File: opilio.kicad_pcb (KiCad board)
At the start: 4 copper layers, 75 x 46 mm, 113 parts, among them J1 Conn_01x04_Male, J2 SATA_Power_Connector, J3 USB_C_Receptacle_USB2.0, J4 Conn_01x06_Male, Q1 CJ3134KW, Q2 AO3401A, Q3 CJ3134KW, Q4 AO3401A, SW1 TS-1077S-01726, SW2 TS-1077S-01726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

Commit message: cleanup
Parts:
- added kibuzzard-638B7105: G***, kibuzzard-638B7105, F.Cu at (109.0, 126.7)
- added kibuzzard-638B7145: G***, kibuzzard-638B7145, F.Cu at (109.6, 130.1)
- added kibuzzard-638BCC66: G***, kibuzzard-638BCC66, F.Cu at (118.7, 99.1)
- moved kibuzzard-63853CA9 1.31 mm to (143.7, 127.1)
- moved kibuzzard-63853BC6 0.16 mm to (117.4, 102.2)
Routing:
- net GND: track 98.2 -> 96.7 mm, vias 82 -> 87
- net WATER_OUT_T: track 17.0 -> 16.3 mm
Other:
- board text added: "3v3"
- board text removed: "VID 0x1209 PID 0x2442"

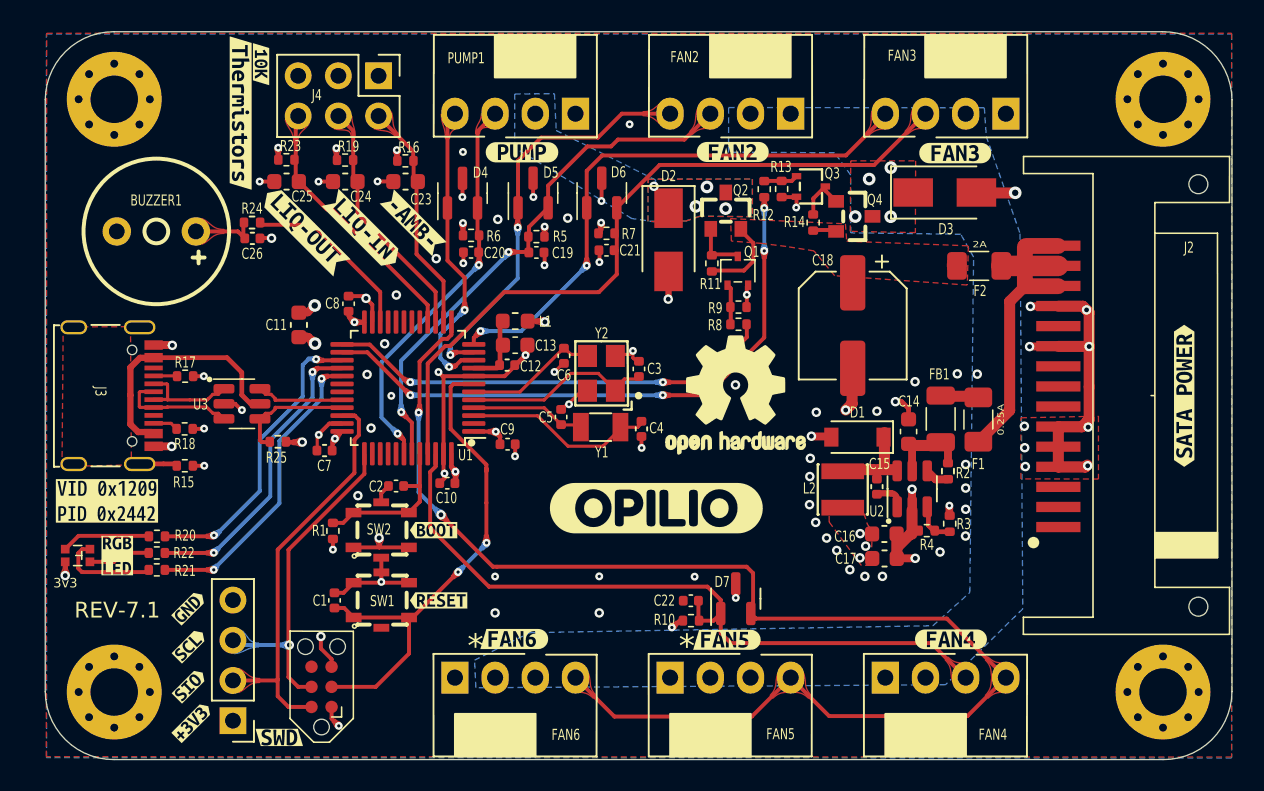
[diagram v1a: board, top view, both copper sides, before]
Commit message: move buzzer and teardrop
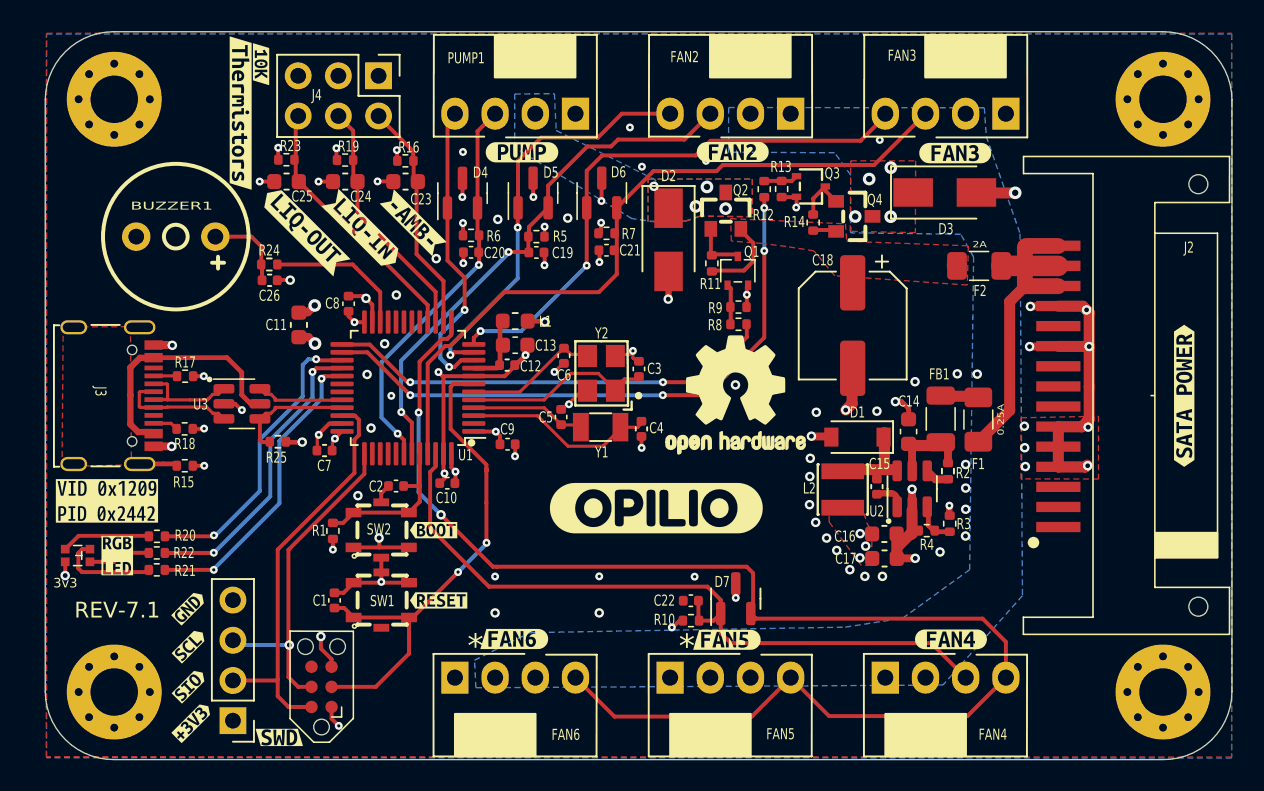
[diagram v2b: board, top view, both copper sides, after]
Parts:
- moved C26 2.87 mm to (119.3, 112.7)
- moved R24 2.87 mm to (119.2, 111.7)
- moved BUZZER1 1.27 mm to (113.3, 110.0)
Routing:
- net BUZZER: track 11.3 -> 9.13 mm
- net PWM_OUT4: track 86.5 -> 87.8 mm
- net Net-(BUZZER1-Pad1): track 4.24 -> 5.32 mm
- net GND: vias 87 -> 91

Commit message: Initial stl files working
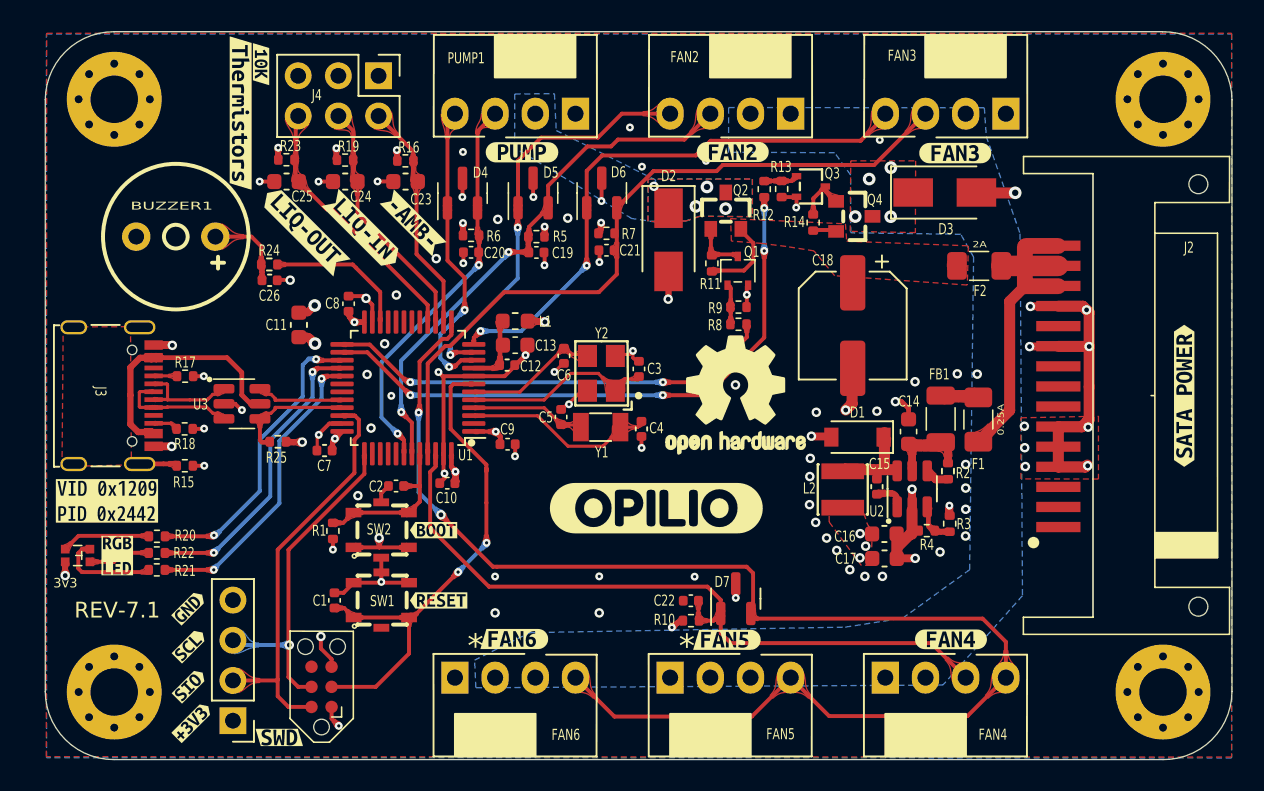
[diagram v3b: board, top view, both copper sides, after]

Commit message: kicad - 7
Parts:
- removed kibuzzard-63853BFA: G***, kibuzzard-63853BFA
- removed kibuzzard-63853C04: G***, kibuzzard-63853C04
- removed kibuzzard-638555C7: G***, kibuzzard-638555C7
- removed kibuzzard-638555D0: G***, kibuzzard-638555D0
- removed kibuzzard-638555D8: G***, kibuzzard-638555D8
- added kibuzzard-63BAEB9A: G***, kibuzzard-63BAEB9A, F.Cu at (123.4, 99.1)
- added kibuzzard-63BAEBBB: G***, kibuzzard-63BAEBBB, F.Cu at (128.5, 99.1)
- added kibuzzard-63BAEC58: G***, kibuzzard-63BAEC58, F.Cu at (126.0, 99.1)
- added kibuzzard-63BAF879: G***, kibuzzard-63BAF879, F.Cu at (126.1, 131.3)
- added kibuzzard-63BAF885: G***, kibuzzard-63BAF885, F.Cu at (133.8, 131.3)
- J4: footprint Connector_PinHeader_2.54mm:PinHeader_2x03_P2.54mm_Vertical -> easyeda2kicad:HDR-TH_6P-P2.54-H-M-R2-C3-S2.54
- moved SW1 8.83 mm to (133.9, 128.4), turned to 180 degrees
- moved C1 7.30 mm to (126.2, 139.7), turned to -90 degrees
- moved J4 7.03 mm to (124.7, 106.7), turned to 180 degrees
- moved R23 6.31 mm to (121.5, 111.3)
- moved R19 6.22 mm to (124.8, 111.3)
- moved R16 6.12 mm to (127.9, 111.3)
- moved C25 3.48 mm to (121.0, 109.9)
- moved C23 3.45 mm to (127.5, 109.9)
- moved C24 3.44 mm to (124.3, 109.9)
- moved kibuzzard-638BCC66 1.43 mm to (120.2, 99.2)
- moved kibuzzard-63853BC6 1.42 mm to (118.8, 102.2)
- moved R24 1.37 mm to (119.2, 113.1)
- moved C26 0.91 mm to (119.2, 111.8)
- moved R13 0.18 mm to (151.4, 107.0)
- moved C8 0.15 mm to (124.2, 114.4)
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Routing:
- net AMBIENT_T: track 14.4 -> 8.96 mm
- net NRST: track 34.6 -> 30.1 mm
- net WATER_IN_T: track 15.3 -> 11.0 mm
- net GND: track 96.7 -> 93.3 mm, vias 91 -> 89
- net PWM_OUT4: track 87.8 -> 90.9 mm
- net WATER_OUT_T: track 16.3 -> 13.4 mm
- net PWM_READ4: track 46.6 -> 47.8 mm
- net BUZZER: track 9.13 -> 8.57 mm
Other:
- board text added: "REV-7.2"
- board text removed: "REV-7.1"

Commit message: enclosure update
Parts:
- moved LOGO1 25.2 mm to (131.6, 138.5)
- moved kibuzzard-63853C0D 8.94 mm to (143.7, 135.4)
- moved FAN6 7.40 mm to (142.2, 137.8)
- moved PUMP1 7.40 mm to (142.2, 102.2)
- moved kibuzzard-63853C81 7.18 mm to (142.4, 104.5)
- moved kibuzzard-638559F0 6.74 mm to (154.9, 135.4)
- moved kibuzzard-63853C76 5.62 mm to (154.2, 104.7)
- moved FAN2 5.00 mm to (153.4, 102.2)
- moved FAN5 5.00 mm to (153.4, 137.8)
- moved FAN3 2.60 mm to (164.6, 102.2)
- moved FAN4 2.60 mm to (164.6, 137.8)
- moved kibuzzard-638559F7 2.43 mm to (164.8, 135.4)
- moved kibuzzard-63853C6A 1.96 mm to (164.6, 104.7)
- moved kibuzzard-63853CA9 0.80 mm to (144.3, 126.7)
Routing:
- net PWM_OUT2: track 26.4 -> 38.5 mm, vias 2 -> 3
- net PWM_OUT1: track 18.6 -> 30.0 mm, vias 2 -> 3
- net PWM_READ1: track 25.0 -> 33.4 mm
- net PWM_READ2: track 33.9 -> 39.8 mm
- net PWM_OUT4: track 90.9 -> 85.6 mm
- net PWM_READ4: track 47.8 -> 50.4 mm
- net PWM_OUT3: track 35.7 -> 38.3 mm
- net PWM_READ3: track 46.2 -> 48.6 mm
- net GND: track 93.3 -> 92.9 mm, vias 89 -> 85
- net 12vP: vias 4 -> 3

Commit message: wip migrate to kicad 7
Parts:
- moved kibuzzard-638559F7 0.12 mm to (164.6, 135.4)
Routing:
- net NRST: track 30.1 -> 31.1 mm

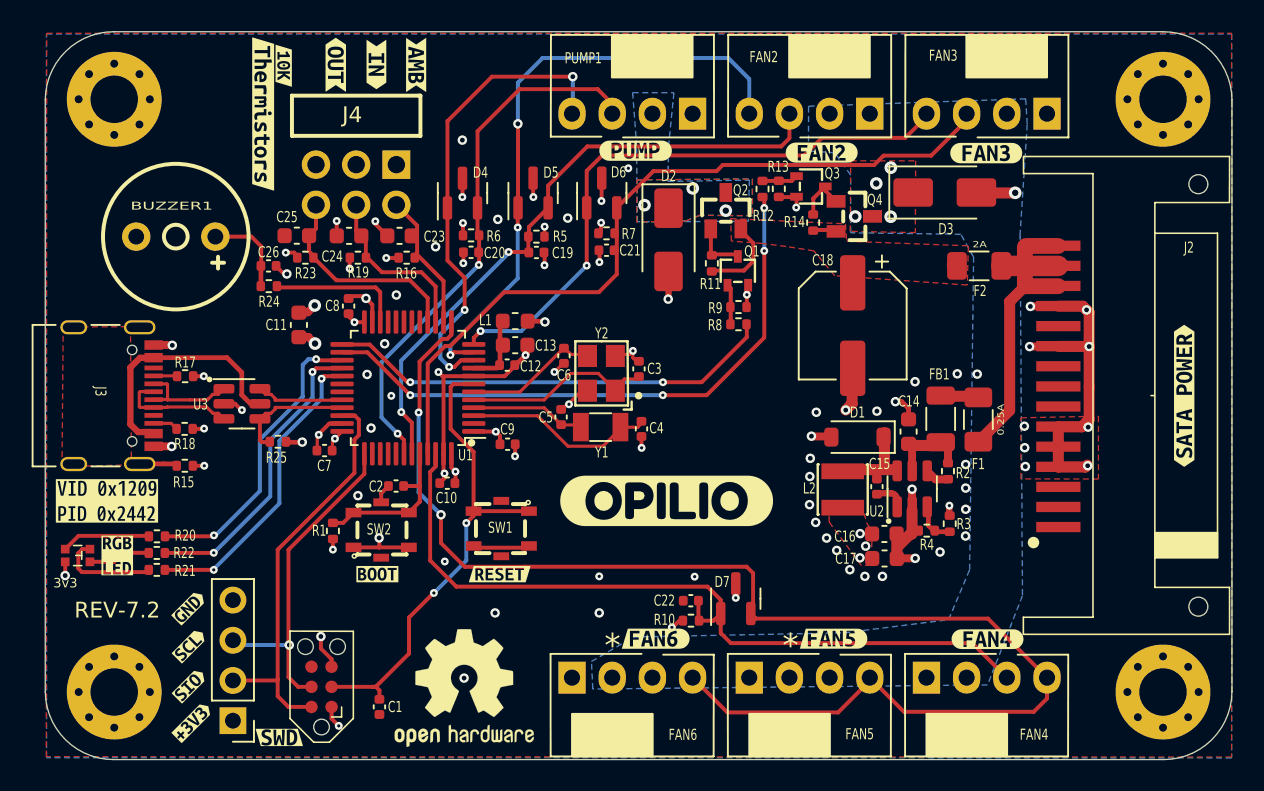
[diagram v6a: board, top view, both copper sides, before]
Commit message: migrated to kicad-7
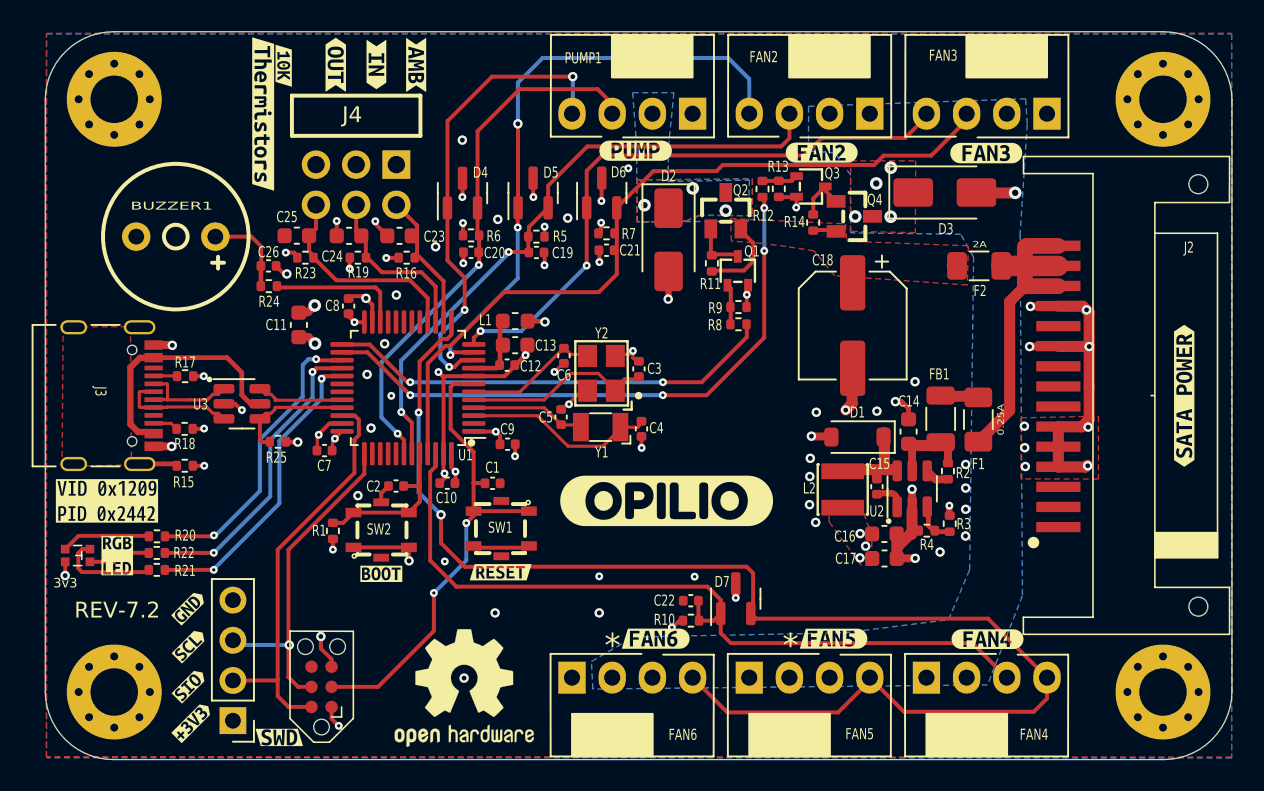
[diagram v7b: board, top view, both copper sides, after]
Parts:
- moved C1 15.8 mm to (133.3, 125.6), turned to 0 degrees
- moved kibuzzard-63BAF879 0.25 mm to (126.3, 131.3)
- moved kibuzzard-63BAF885 0.13 mm to (133.9, 131.2)
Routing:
- net GND: vias 85 -> 78
- added copper zone on In2.Cu, net 12vC
- added copper zone on In2.Cu, net 12vP

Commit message: almost ready for order
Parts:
- added FID1: Fiducial, Fiducial:Fiducial_0.5mm_Mask1mm, F.Cu at (150.6, 120.0)
- added FID2: Fiducial, Fiducial:Fiducial_0.5mm_Mask1mm, F.Cu at (172.6, 120.0)
- added FID3: Fiducial, Fiducial:Fiducial_0.5mm_Mask1mm, F.Cu at (114.6, 102.0)
- moved R11 1.87 mm to (149.0, 111.3), turned to -90 degrees
- moved Q1 1.51 mm to (147.6, 112.9)
- moved R8 1.46 mm to (147.6, 116.1)
- moved R9 1.46 mm to (147.6, 115.0)
- moved C2 0.46 mm to (126.8, 125.7)
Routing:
- net +12VF(F): track 6.58 -> 2.72 mm
- net Net-(Q1-G): track 4.91 -> 2.31 mm
- net PUMP_EN: track 28.5 -> 27.4 mm
- net Net-(Q1-D): track 3.48 -> 4.26 mm
- net GND: track 92.9 -> 92.5 mm, vias 78 -> 77
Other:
- board text added: "REV-8"
- board text removed: "REV-7.2"
